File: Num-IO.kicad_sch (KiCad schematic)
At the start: 25 parts, among them J10 DB25_Female, J5 Conn_01x02_Male, J6 Conn_01x02_Male, J7 Conn_01x02_Male, U14 HCPL-063A, U3 MAX14851AEE+

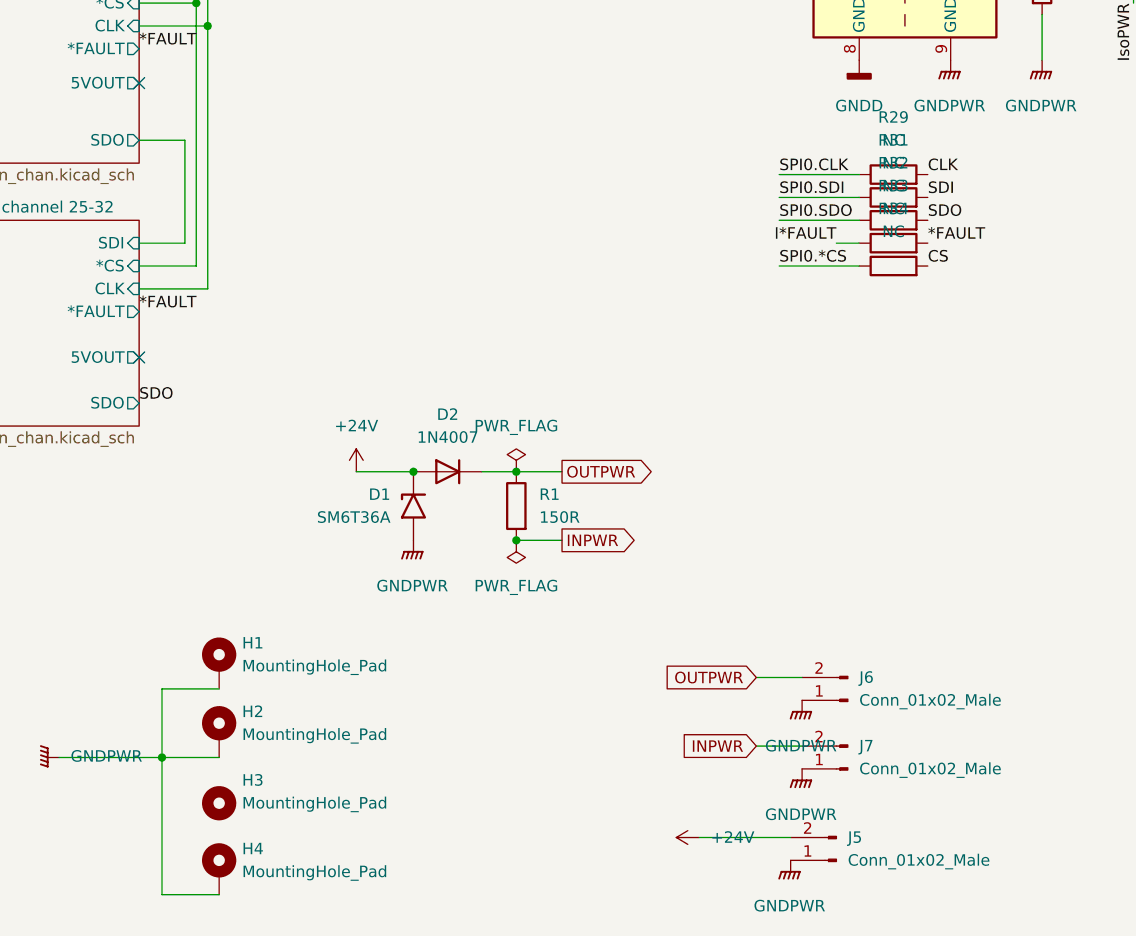
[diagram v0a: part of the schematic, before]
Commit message: add zeners in the meantime, if the SPI isolator is delayed
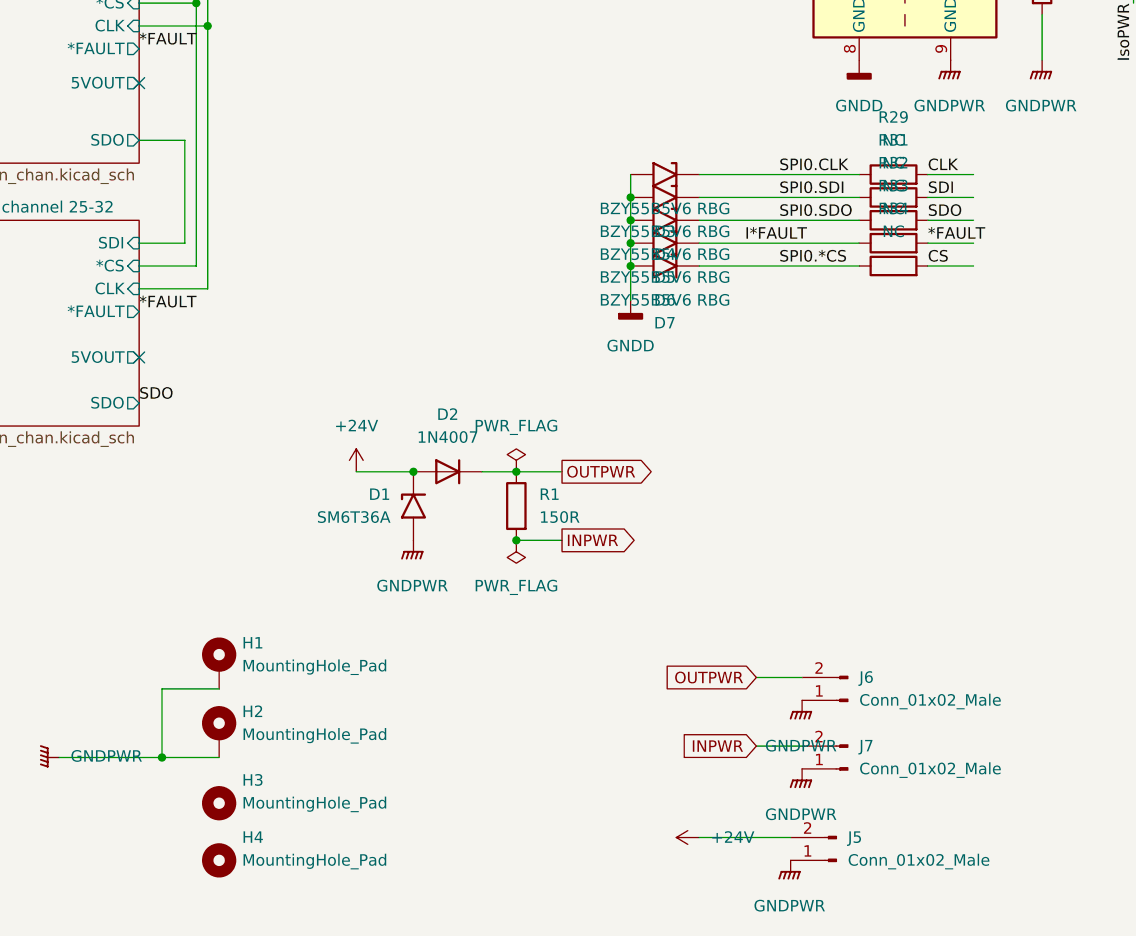
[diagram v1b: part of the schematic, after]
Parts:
- removed H4: MountingHole_Pad, MountingHole:MountingHole_3.2mm_M3_DIN965_Pad, symbol Mechanical:MountingHole_Pad
- added D3, D4, D5, D6, D7: BZY55B5V6 RBG, Diode_SMD:D_0805_2012Metric, symbol Diode:SM6T36A
- added H4: MountingHole_Pad, MountingHole:MountingHole_3.2mm_M3_DIN965_Pad, symbol Mechanical:MountingHole
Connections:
- net GNDD: now also D3.2 (A2), D4.2 (A2), D5.2 (A2), D6.2 (A2), D7.2 (A2)
- net I*FAULT: now also D6.1 (A1)
- net SPI0.*CS: now also D7.1 (A1)
- net SPI0.CLK: now also D3.1 (A1)
- net SPI0.SDI: now also D4.1 (A1)
- net SPI0.SDO: now also D5.1 (A1)

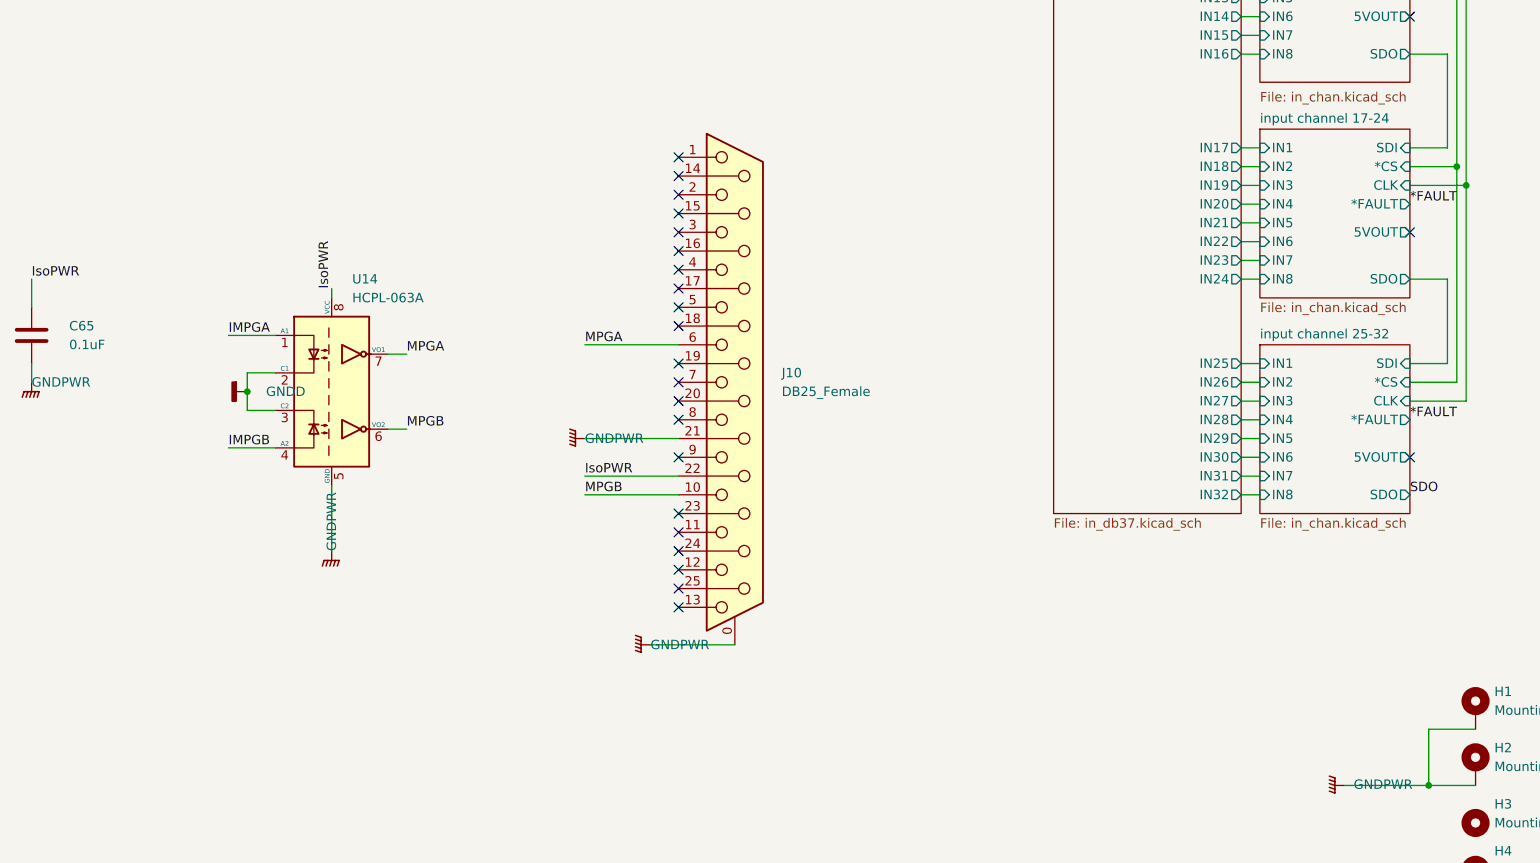
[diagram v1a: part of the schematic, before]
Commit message: move MPG to dedicated file
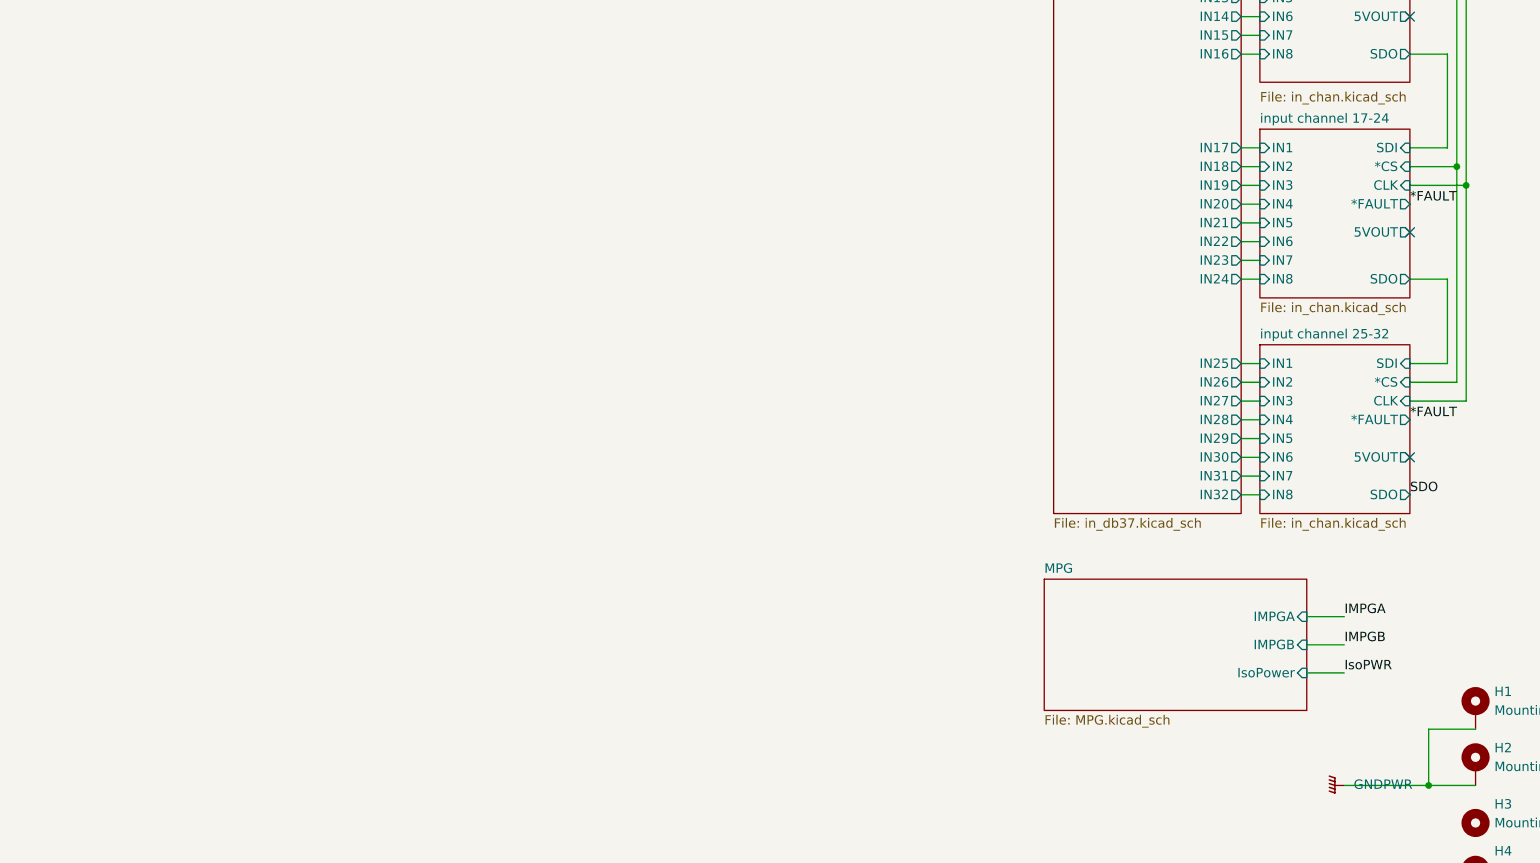
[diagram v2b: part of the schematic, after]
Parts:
- removed C65: 0.1uF, Capacitor_SMD:C_0805_2012Metric, symbol Device:C
- removed J10: DB25_Female, Connector_Dsub:DSUB-25_Female_Vertical_P2.77x2.84mm_MountingHoles, symbol Connector:DB25_Female_MountingHoles
- removed U14: HCPL-063A, Package_SO:SOIC-8_3.9x4.9mm_P1.27mm, symbol Isolator:HCPL-063A
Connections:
- no-connect marks 27 -> 6
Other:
- added sheet MPG (MPG.kicad_sch)

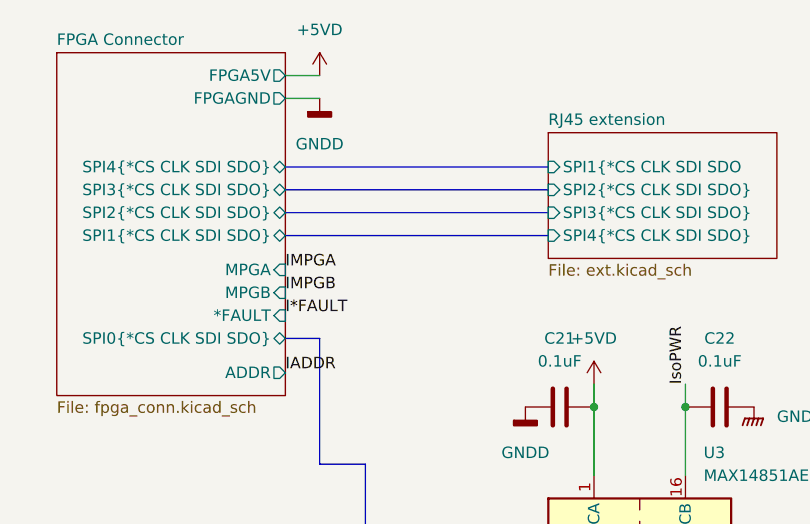
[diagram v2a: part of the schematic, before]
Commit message: remove 5V (now 3.3V) + tuning
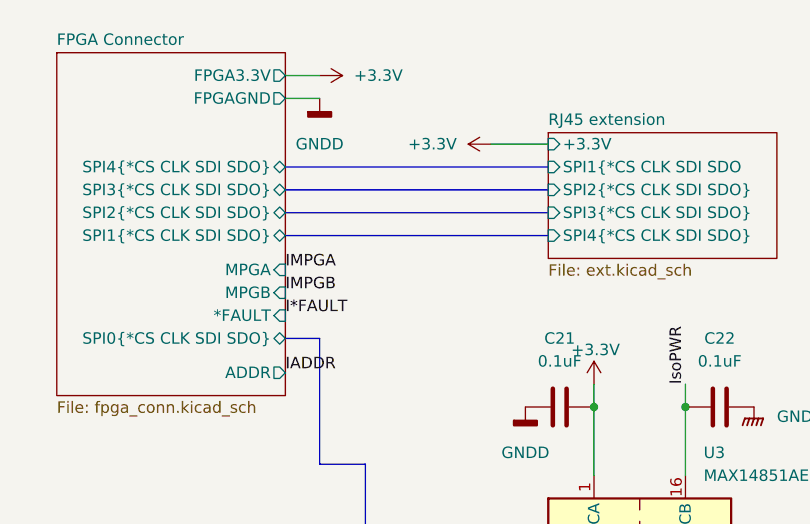
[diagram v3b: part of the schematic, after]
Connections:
- net +5VD renamed +3V3
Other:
- sheet FPGA Connector ports: added FPGA3.3V; removed FPGA5V
- sheet RJ45 extension ports: added +3.3V; removed none

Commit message: fix warnings
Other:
- sheet RJ45 extension ports: added power; removed +3.3V
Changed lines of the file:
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@@
       (effects (font (size 1.27 1.27)) (justify left))
     )
-    (pin "+3.3V" input (at 140.97 27.94 180)
+    (pin "power" input (at 140.97 27.94 180)
       (effects (font (size 1.27 1.27)) (justify left))
     )
@@
       (reference "#PWR010") (unit 1) (value "+24V") (footprint "")
     )
-    (path "/1d55f859-b955-4956-adf8-4e32f584531b/170ad15f-26c7-4c22-a90c-54623ee4402d"
-      (reference "#PWR011") (unit 1) (value "+3.3V") (footprint "")
-    )
     (path "/b07b96d9-6f40-4a2b-83cd-f9b64e58323a"
       (reference "#PWR012") (unit 1) (value "GNDD") (footprint "")
@@
       (reference "#PWR094") (unit 1) (value "GNDPWR") (footprint "")
     )
-    (path "/1d55f859-b955-4956-adf8-4e32f584531b/b132ec1f-11c2-46f1-b941-9d8d354ace60"
-      (reference "#PWR0101") (unit 1) (value "+3.3V") (footprint "")
-    )
-    (path "/1d55f859-b955-4956-adf8-4e32f584531b/3453f1f4-d6cc-4530-8674-55e70efacfe8"
-      (reference "#PWR0102") (unit 1) (value "+3.3V") (footprint "")
-    )
-    (path "/1d55f859-b955-4956-adf8-4e32f584531b/de7438a7-6961-4873-9d60-eaa34b613b97"
-      (reference "#PWR0103") (unit 1) (value "+3.3V") (footprint "")
-    )
     (path "/1d55f859-b955-4956-adf8-4e32f584531b/86598639-dfdd-4e36-a77a-c830bedc9aee"
       (reference "#PWR0104") (unit 1) (value "GNDD") (footprint "")
@@
       (reference "#PWR0106") (unit 1) (value "GNDD") (footprint "")
     )
-    (path "/1d55f859-b955-4956-adf8-4e32f584531b/4669e027-83a2-4fb6-8a98-866098ea7982"
-      (reference "#PWR0107") (unit 1) (value "+3.3V") (footprint "")
-    )
-    (path "/1d55f859-b955-4956-adf8-4e32f584531b/65065733-7b3f-4090-9a30-44385e7fb45b"
-      (reference "#PWR0108") (unit 1) (value "+3.3V") (footprint "")
-    )
     (path "/1d55f859-b955-4956-adf8-4e32f584531b/5a3f0d04-2157-4136-a203-e229fc65cd9c"
       (reference "#PWR0109") (unit 1) (value "GNDD") (footprint "")
@@
       (reference "#PWR0110") (unit 1) (value "GNDD") (footprint "")
     )
-    (path "/1d55f859-b955-4956-adf8-4e32f584531b/4ee6171d-eeef-4072-879d-95ce91b8bbfe"
-      (reference "#PWR0111") (unit 1) (value "+3.3V") (footprint "")
-    )
     (path "/1d55f859-b955-4956-adf8-4e32f584531b/38188175-a9f3-4dce-a140-938c28e53d63"
       (reference "#PWR0112") (unit 1) (value "GNDD") (footprint "")
     )
-    (path "/1d55f859-b955-4956-adf8-4e32f584531b/fc417dd9-3de8-49c5-9a9a-3fc9e14e263c"
-      (reference "#PWR0113") (unit 1) (value "+3.3V") (footprint "")
-    )
     (path "/1d55f859-b955-4956-adf8-4e32f584531b/c50bb327-78ee-44e5-9ab4-e923f9624baf"
       (reference "#PWR0114") (unit 1) (value "GNDD") (footprint "")
     )
-    (path "/1d55f859-b955-4956-adf8-4e32f584531b/f3d42df9-a8c6-4c3a-84b1-022f948bbca4"
-      (reference "#PWR0115") (unit 1) (value "+3.3V") (footprint "")
-    )
     (path "/1d55f859-b955-4956-adf8-4e32f584531b/0dc32d75-f36e-4b14-aafe-2cc894f786db"
       (reference "#PWR0116") (unit 1) (value "GNDD") (footprint "")
     )
-    (path "/1d55f859-b955-4956-adf8-4e32f584531b/18c510f3-671b-4fd6-b9dd-99e163a6a52e"
-      (reference "#PWR0118") (unit 1) (value "+3.3V") (footprint "")
-    )
-    (path "/1d55f859-b955-4956-adf8-4e32f584531b/720ef364-414d-4000-92f8-05b8d8ef0c30"
-      (reference "#PWR0119") (unit 1) (value "+3.3V") (footprint "")
-    )
-    (path "/1d55f859-b955-4956-adf8-4e32f584531b/ca5bafa4-ce44-4686-bd1b-ca5d1303c0d0"
-      (reference "#PWR0120") (unit 1) (value "+3.3V") (footprint "")
-    )
-    (path "/1d55f859-b955-4956-adf8-4e32f584531b/29161174-fb07-48d1-816b-94d43f35969c"
-      (reference "#PWR0121") (unit 1) (value "+3.3V") (footprint "")
-    )
-    (path "/1d55f859-b955-4956-adf8-4e32f584531b/fa5c9950-ad07-42da-bc40-98af17e8ac23"
-      (reference "#PWR0122") (unit 1) (value "+3.3V") (footprint "")
-    )
-    (path "/1d55f859-b955-4956-adf8-4e32f584531b/5a33b897-7b10-40c1-a35f-26e888bd961c"
-      (reference "#PWR0123") (unit 1) (value "+3.3V") (footprint "")
-    )
-    (path "/1d55f859-b955-4956-adf8-4e32f584531b/787dc7bb-72e3-4c35-8fac-6ca6adc24882"
-      (reference "#PWR0124") (unit 1) (value "+3.3V") (footprint "")
-    )
-    (path "/1d55f859-b955-4956-adf8-4e32f584531b/02152c4e-8ce7-4522-bde2-9508b3590893"
-      (reference "#PWR0125") (unit 1) (value "+3.3V") (footprint "")
-    )
-    (path "/1d55f859-b955-4956-adf8-4e32f584531b/d858782c-2446-4e9e-8df0-05f5deb9f112"
-      (reference "#PWR0126") (unit 1) (value "+3.3V") (footprint "")
-    )
-    (path "/1d55f859-b955-4956-adf8-4e32f584531b/13162186-7362-4f87-96f7-d05f4258dc20"
-      (reference "#PWR0127") (unit 1) (value "+3.3V") (footprint "")
-    )
-    (path "/1d55f859-b955-4956-adf8-4e32f584531b/9d2aed28-672a-4c6c-8df5-e3eb55e83acc"
-      (reference "#PWR0128") (unit 1) (value "+3.3V") (footprint "")
-    )
-    (path "/1d55f859-b955-4956-adf8-4e32f584531b/6e8e240d-89d6-428f-9655-5761a71cb0ea"
-      (reference "#PWR0129") (unit 1) (value "+3.3V") (footprint "")
-    )
-    (path "/1d55f859-b955-4956-adf8-4e32f584531b/3689f931-8e4c-4e2d-a269-a4ee2a4de4d3"
-      (reference "#PWR0130") (unit 1) (value "+3.3V") (footprint "")
-    )
     (path "/1d55f859-b955-4956-adf8-4e32f584531b/375f888c-0b25-4078-9e28-dcd15169d0c9"
       (reference "#PWR0131") (unit 1) (value "GNDD") (footprint "")
@@
       (reference "#PWR0144") (unit 1) (value "+3.3V") (footprint "")
     )
-    (path "/1d55f859-b955-4956-adf8-4e32f584531b/802c3014-7ad8-48bd-8a88-8dfe884f82ef"
-      (reference "#PWR0145") (unit 1) (value "+3.3V") (footprint "")
-    )
     (path "/94eb0688-f710-4c77-a991-98d54924db98/12393bb7-cbb7-41d4-afd0-c2062de5fe4c"
